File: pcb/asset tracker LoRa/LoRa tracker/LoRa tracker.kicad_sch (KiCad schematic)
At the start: 9 parts

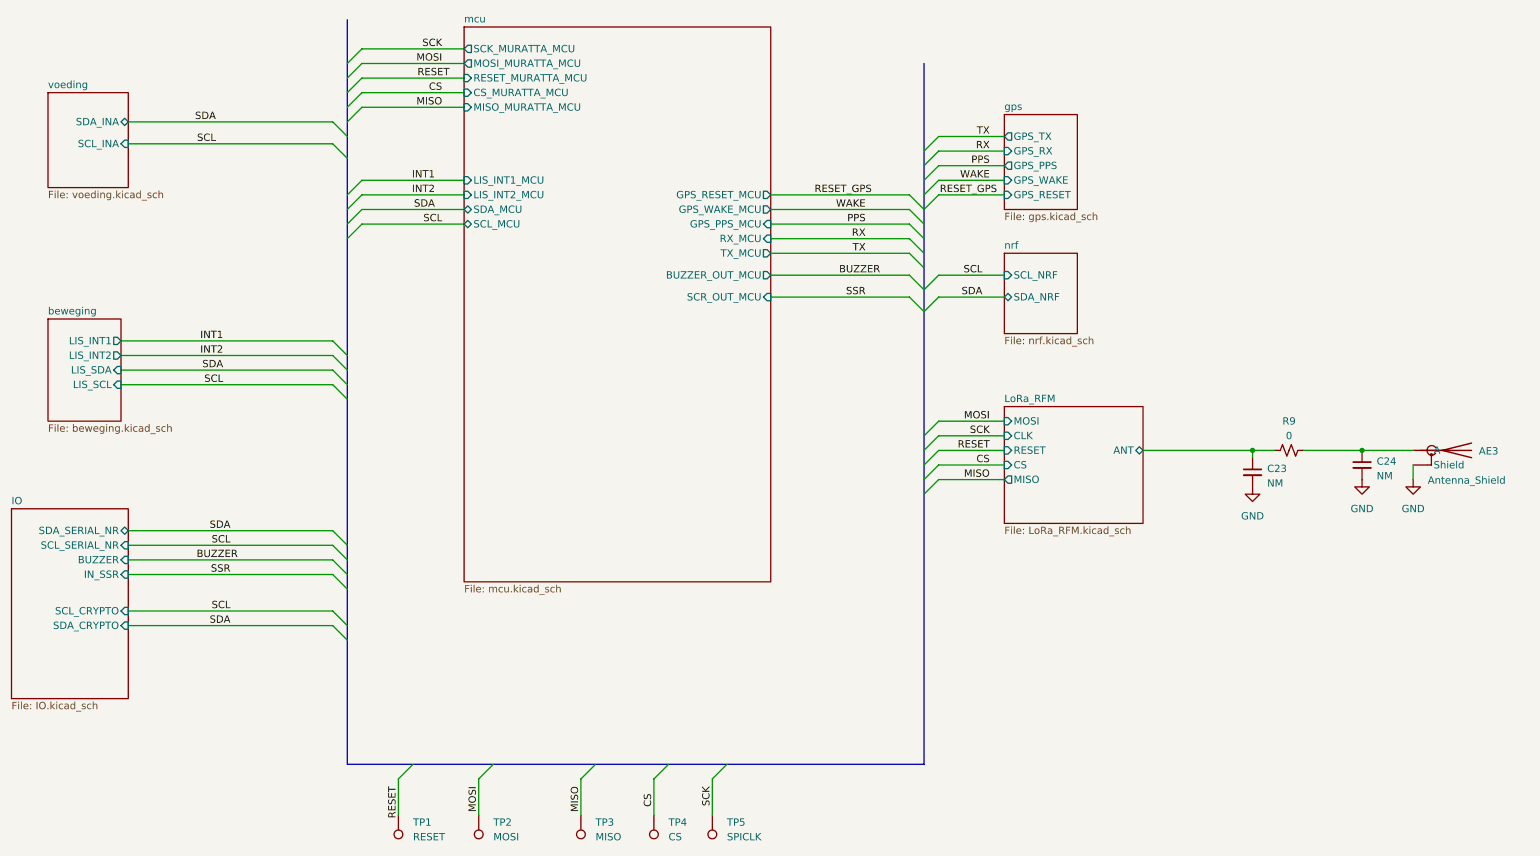
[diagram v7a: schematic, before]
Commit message: versie2
aan versie 2 begonnen met tekenen en code beginnen schrijven voor quadkey
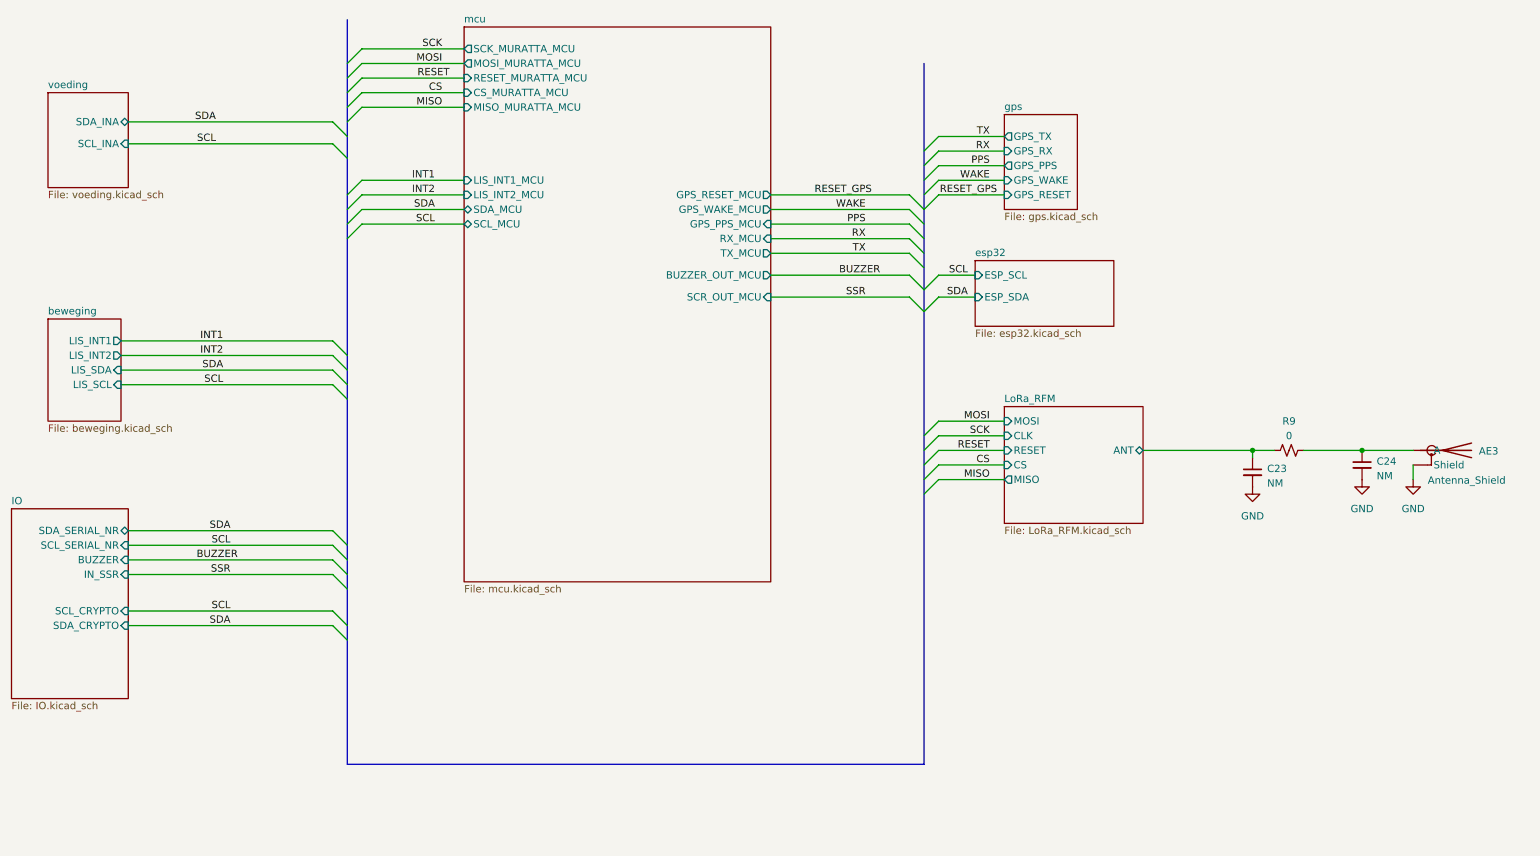
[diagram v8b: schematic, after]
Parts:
- removed TP1: RESET, vanalles:TestPoint_Pad_D3.0mm, symbol Connector:Test_Point
- removed TP2: MOSI, vanalles:TestPoint_Pad_D3.0mm, symbol Connector:Test_Point
- removed TP3: MISO, vanalles:TestPoint_Pad_D3.0mm, symbol Connector:Test_Point
- removed TP4: CS, vanalles:TestPoint_Pad_D3.0mm, symbol Connector:Test_Point
- removed TP5: SPICLK, vanalles:TestPoint_Pad_D3.0mm, symbol Connector:Test_Point
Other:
- removed sheet nrf
- added sheet esp32 (esp32.kicad_sch)
